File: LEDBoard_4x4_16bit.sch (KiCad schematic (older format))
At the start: 34 parts, among them J1 VCC_in, J2 GND_in, J3 signal_in, J4 VCC_out, J5 GND_out, J6 signal_out, U1 TLC5971RGER, U2 TLC5971RGER, U3 TLC5971RGER, U4 TLC5971RGER

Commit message: pcb parts all positioned
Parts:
- removed J2: GND_in, Socket_Strips:Socket_Strip_Angled_1x01_Pitch2.54mm, symbol CONN_01X01_MALE
- removed J4: VCC_out, Socket_Strips:Socket_Strip_Angled_1x01_Pitch2.54mm, symbol CONN_01X01_FEMALE
- removed J5: GND_out, Socket_Strips:Socket_Strip_Angled_1x01_Pitch2.54mm, symbol CONN_01X01_FEMALE
- added C5: 47uF, Capacitors_SMD:C_0603, symbol C
- added HS1: Heatsink, Oddities:Dummy_Empty, symbol Heatsink
- added MK1, MK2: Mounting_Hole, Mounting_Holes:MountingHole_2.7mm_M2.5_Pad_Via, symbol Mounting_Hole_PAD
- C1: YAGEO (none) -> CC0603KRX7R7BB104; reichelt (none) -> X7R-G0603 100N; reichelt_url (none) -> https://www.reichelt.de/Vielschicht-SMD-G0603/X7R-G0603-100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
- J2: renamed from J1; value VCC_in -> power; footprint Socket_Strips:Socket_Strip_Angled_1x01_Pitch2.54mm -> Socket_Strips:Socket_Strip_Straight_1x06_Pitch2.54mm; symbol CONN_01X01_MALE -> CONN_01X06
- J6: footprint Socket_Strips:Socket_Strip_Angled_1x02_Pitch2.54mm -> Socket_Strips:Socket_Strip_Straight_1x02_Pitch2.54mm
- R1: value R -> 2k7 1%; YAGEO (none) -> RC0603FR-072K7L; reichelt (none) -> SMD-0603 2,7K; reichelt_url (none) -> https://www.reichelt.de/SMD-0603-von-1-bis-910-kOhm/SMD-060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
- U1, U2, U3, U4: footprint Housings_DFN_QFN:QFN-24-1EP_4x4mm_Pitch0.5mm -> Housings_DFN_QFN:Texas_S-PVQFN-N24_ThermalVias
- renumbered J3 to J1
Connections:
- wire segments 66 -> 74
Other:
- moved on the sheet: J1, J6

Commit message: pcb started routing
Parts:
- D1.1, D1.2, D1.3, D1.4, D2.1, D2.2, D2.3, D2.4, D3.1, D3.2, D3.3, D3.4, D4.1, D4.2, D4.3, D4.4: footprint nichia:LED_NSSM032AT_wViaHeatSink -> nichia:LED_NSSM032AT_wViaHeatSinkBig
- MK1, MK2: footprint Mounting_Holes:MountingHole_2.7mm_M2.5_Pad_Via -> Mounting_Holes:MountingHole_3.2mm_M3_ISO7380_Pad
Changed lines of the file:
@@
 F 0 "D1.1" H 3950 2047 50  0000 C CNN
 F 1 "LED_1.1" H 3950 1956 50  0000 C CNN
-F 2 "nichia:LED_NSSM032AT_wViaHeatSink" H 3950 1500 50  0001 C CNN
+F 2 "nichia:LED_NSSM032AT_wViaHeatSinkBig" H 3950 1500 50  0001 C CNN
 F 3 "" H 3950 1500 50  0001 C CNN
 F 4 "NSSM032A" H 3950 1550 60  0001 C CNN "Nichia part"
@@
 F 0 "D1.2" H 3950 2947 50  0000 C CNN
 F 1 "LED_1.2" H 3950 2856 50  0000 C CNN
-F 2 "nichia:LED_NSSM032AT_wViaHeatSink" H 3950 2400 50  0001 C CNN
+F 2 "nichia:LED_NSSM032AT_wViaHeatSinkBig" H 3950 2400 50  0001 C CNN
 F 3 "" H 3950 2400 50  0001 C CNN
 F 4 "NSSM032A" H 3950 2450 60  0001 C CNN "Nichia part"
@@
 F 0 "D2.1" H 5150 2047 50  0000 C CNN
 F 1 "LED_2.1" H 5150 1956 50  0000 C CNN
-F 2 "nichia:LED_NSSM032AT_wViaHeatSink" H 5150 1500 50  0001 C CNN
+F 2 "nichia:LED_NSSM032AT_wViaHeatSinkBig" H 5150 1500 50  0001 C CNN
 F 3 "" H 5150 1500 50  0001 C CNN
 F 4 "NSSM032A" H 5150 1550 60  0001 C CNN "Nichia part"
@@
 F 0 "D2.2" H 5150 2947 50  0000 C CNN
 F 1 "LED_2.2" H 5150 2856 50  0000 C CNN
-F 2 "nichia:LED_NSSM032AT_wViaHeatSink" H 5150 2400 50  0001 C CNN
+F 2 "nichia:LED_NSSM032AT_wViaHeatSinkBig" H 5150 2400 50  0001 C CNN
 F 3 "" H 5150 2400 50  0001 C CNN
 F 4 "NSSM032A" H 5150 2450 60  0001 C CNN "Nichia part"
@@
 F 0 "D3.1" H 9250 2047 50  0000 C CNN
 F 1 "LED_3.1" H 9250 1956 50  0000 C CNN
-F 2 "nichia:LED_NSSM032AT_wViaHeatSink" H 9250 1500 50  0001 C CNN
+F 2 "nichia:LED_NSSM032AT_wViaHeatSinkBig" H 9250 1500 50  0001 C CNN
 F 3 "" H 9250 1500 50  0001 C CNN
 F 4 "NSSM032A" H 9250 1550 60  0001 C CNN "Nichia part"
@@
 F 0 "D3.2" H 9250 2947 50  0000 C CNN
 F 1 "LED_3.2" H 9250 2856 50  0000 C CNN
-F 2 "nichia:LED_NSSM032AT_wViaHeatSink" H 9250 2400 50  0001 C CNN
+F 2 "nichia:LED_NSSM032AT_wViaHeatSinkBig" H 9250 2400 50  0001 C CNN
 F 3 "" H 9250 2400 50  0001 C CNN
 F 4 "NSSM032A" H 9250 2450 60  0001 C CNN "Nichia part"
@@
 F 0 "D4.1" H 10450 2047 50  0000 C CNN
 F 1 "LED_4.1" H 10450 1956 50  0000 C CNN
-F 2 "nichia:LED_NSSM032AT_wViaHeatSink" H 10450 1500 50  0001 C CNN
+F 2 "nichia:LED_NSSM032AT_wViaHeatSinkBig" H 10450 1500 50  0001 C CNN
 F 3 "" H 10450 1500 50  0001 C CNN
 F 4 "NSSM032A" H 10450 1550 60  0001 C CNN "Nichia part"
@@
 F 0 "D4.2" H 10450 2947 50  0000 C CNN
 F 1 "LED_4.2" H 10450 2856 50  0000 C CNN
-F 2 "nichia:LED_NSSM032AT_wViaHeatSink" H 10450 2400 50  0001 C CNN
+F 2 "nichia:LED_NSSM032AT_wViaHeatSinkBig" H 10450 2400 50  0001 C CNN
 F 3 "" H 10450 2400 50  0001 C CNN
 F 4 "NSSM032A" H 10450 2450 60  0001 C CNN "Nichia part"
@@
 F 0 "D1.3" H 3950 4797 50  0000 C CNN
 F 1 "LED_1.3" H 3950 4706 50  0000 C CNN
-F 2 "nichia:LED_NSSM032AT_wViaHeatSink" H 3950 4250 50  0001 C CNN
+F 2 "nichia:LED_NSSM032AT_wViaHeatSinkBig" H 3950 4250 50  0001 C CNN
 F 3 "" H 3950 4250 50  0001 C CNN
 F 4 "NSSM032A" H 3950 4300 60  0001 C CNN "Nichia part"
@@
 F 0 "D1.4" H 3950 5697 50  0000 C CNN
 F 1 "LED_1.4" H 3950 5606 50  0000 C CNN
-F 2 "nichia:LED_NSSM032AT_wViaHeatSink" H 3950 5150 50  0001 C CNN
+F 2 "nichia:LED_NSSM032AT_wViaHeatSinkBig" H 3950 5150 50  0001 C CNN
 F 3 "" H 3950 5150 50  0001 C CNN
 F 4 "NSSM032A" H 3950 5200 60  0001 C CNN "Nichia part"
@@
 F 0 "D2.3" H 5150 4797 50  0000 C CNN
 F 1 "LED_2.3" H 5150 4706 50  0000 C CNN
-F 2 "nichia:LED_NSSM032AT_wViaHeatSink" H 5150 4250 50  0001 C CNN
+F 2 "nichia:LED_NSSM032AT_wViaHeatSinkBig" H 5150 4250 50  0001 C CNN
 F 3 "" H 5150 4250 50  0001 C CNN
 F 4 "NSSM032A" H 5150 4300 60  0001 C CNN "Nichia part"
@@
 F 0 "D2.4" H 5150 5697 50  0000 C CNN
 F 1 "LED_2.4" H 5150 5606 50  0000 C CNN
-F 2 "nichia:LED_NSSM032AT_wViaHeatSink" H 5150 5150 50  0001 C CNN
+F 2 "nichia:LED_NSSM032AT_wViaHeatSinkBig" H 5150 5150 50  0001 C CNN
 F 3 "" H 5150 5150 50  0001 C CNN
 F 4 "NSSM032A" H 5150 5200 60  0001 C CNN "Nichia part"
@@
 F 0 "D3.3" H 9250 4797 50  0000 C CNN
 F 1 "LED_3.3" H 9250 4706 50  0000 C CNN
-F 2 "nichia:LED_NSSM032AT_wViaHeatSink" H 9250 4250 50  0001 C CNN
+F 2 "nichia:LED_NSSM032AT_wViaHeatSinkBig" H 9250 4250 50  0001 C CNN
 F 3 "" H 9250 4250 50  0001 C CNN
 F 4 "NSSM032A" H 9250 4300 60  0001 C CNN "Nichia part"
@@
 F 0 "D3.4" H 9250 5697 50  0000 C CNN
 F 1 "LED_3.4" H 9250 5606 50  0000 C CNN
-F 2 "nichia:LED_NSSM032AT_wViaHeatSink" H 9250 5150 50  0001 C CNN
+F 2 "nichia:LED_NSSM032AT_wViaHeatSinkBig" H 9250 5150 50  0001 C CNN
 F 3 "" H 9250 5150 50  0001 C CNN
 F 4 "NSSM032A" H 9250 5200 60  0001 C CNN "Nichia part"
@@
 F 0 "D4.3" H 10450 4797 50  0000 C CNN
 F 1 "LED_4.3" H 10450 4706 50  0000 C CNN
-F 2 "nichia:LED_NSSM032AT_wViaHeatSink" H 10450 4250 50  0001 C CNN
+F 2 "nichia:LED_NSSM032AT_wViaHeatSinkBig" H 10450 4250 50  0001 C CNN
 F 3 "" H 10450 4250 50  0001 C CNN
 F 4 "NSSM032A" H 10450 4300 60  0001 C CNN "Nichia part"
@@
 F 0 "D4.4" H 10450 5697 50  0000 C CNN
 F 1 "LED_4.4" H 10450 5606 50  0000 C CNN
-F 2 "nichia:LED_NSSM032AT_wViaHeatSink" H 10450 5150 50  0001 C CNN
+F 2 "nichia:LED_NSSM032AT_wViaHeatSinkBig" H 10450 5150 50  0001 C CNN
 F 3 "" H 10450 5150 50  0001 C CNN
 F 4 "NSSM032A" H 10450 5200 60  0001 C CNN "Nichia part"
@@
 F 0 "MK1" H 4050 6051 50  0000 L CNN
 F 1 "Mounting_Hole" H 4050 5960 50  0000 L CNN
-F 2 "Mounting_Holes:MountingHole_2.7mm_M2.5_Pad_Via" H 3950 6000 50  0001 C CNN
+F 2 "Mounting_Holes:MountingHole_3.2mm_M3_ISO7380_Pad" H 3950 6000 50  0001 C CNN
 F 3 "" H 3950 6000 50  0001 C CNN
 	1    3950 6000
@@
 $EndComp
 $Comp
-L GND #PWR053
+L GND #PWR051
 U 1 1 596BEB36
 P 3950 6100
-F 0 "#PWR053" H 3950 5850 50  0001 C CNN
+F 0 "#PWR051" H 3950 5850 50  0001 C CNN
 F 1 "GND" H 3955 5927 50  0000 C CNN
 F 2 "" H 3950 6100 50  0001 C CNN
@@
 F 0 "MK2" H 4800 6051 50  0000 L CNN
 F 1 "Mounting_Hole" H 4800 5960 50  0000 L CNN
-F 2 "Mounting_Holes:MountingHole_2.7mm_M2.5_Pad_Via" H 4700 6000 50  0001 C CNN
+F 2 "Mounting_Holes:MountingHole_3.2mm_M3_ISO7380_Pad" H 4700 6000 50  0001 C CNN
 F 3 "" H 4700 6000 50  0001 C CNN
 	1    4700 6000
@@
 $EndComp
 $Comp
-L GND #PWR054
+L GND #PWR052
 U 1 1 596BF4D1
 P 4700 6100
-F 0 "#PWR054" H 4700 5850 50  0001 C CNN
+F 0 "#PWR052" H 4700 5850 50  0001 C CNN
 F 1 "GND" H 4705 5927 50  0000 C CNN
 F 2 "" H 4700 6100 50  0001 C CNN

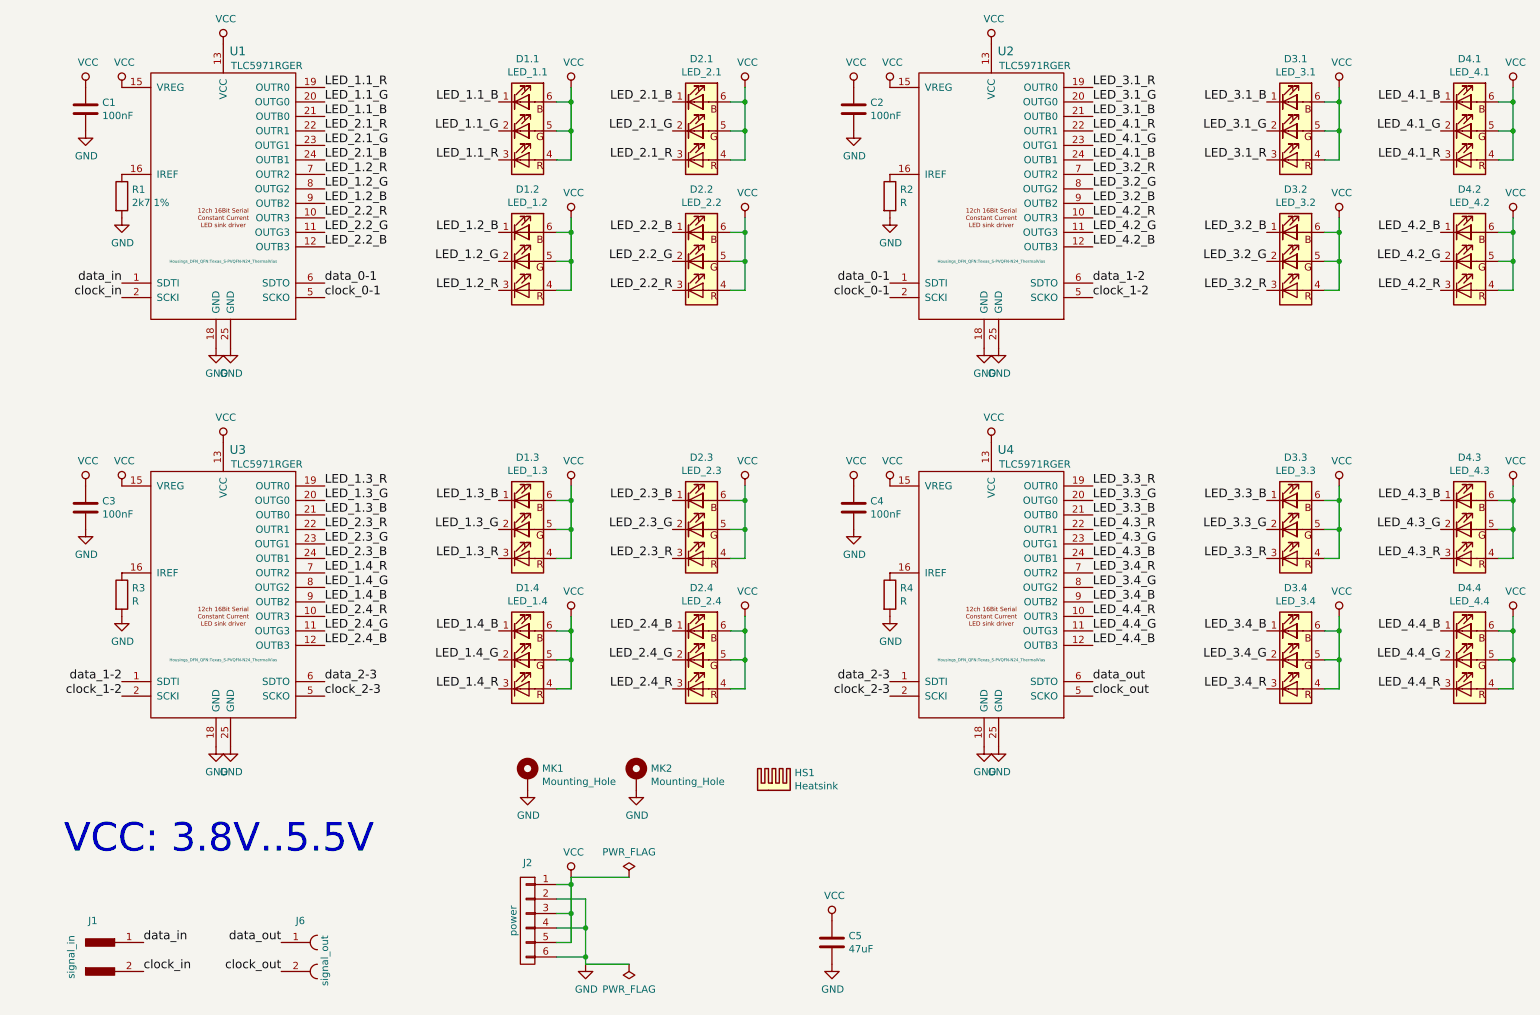
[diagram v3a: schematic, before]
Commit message: pcb tried to fix missing net links
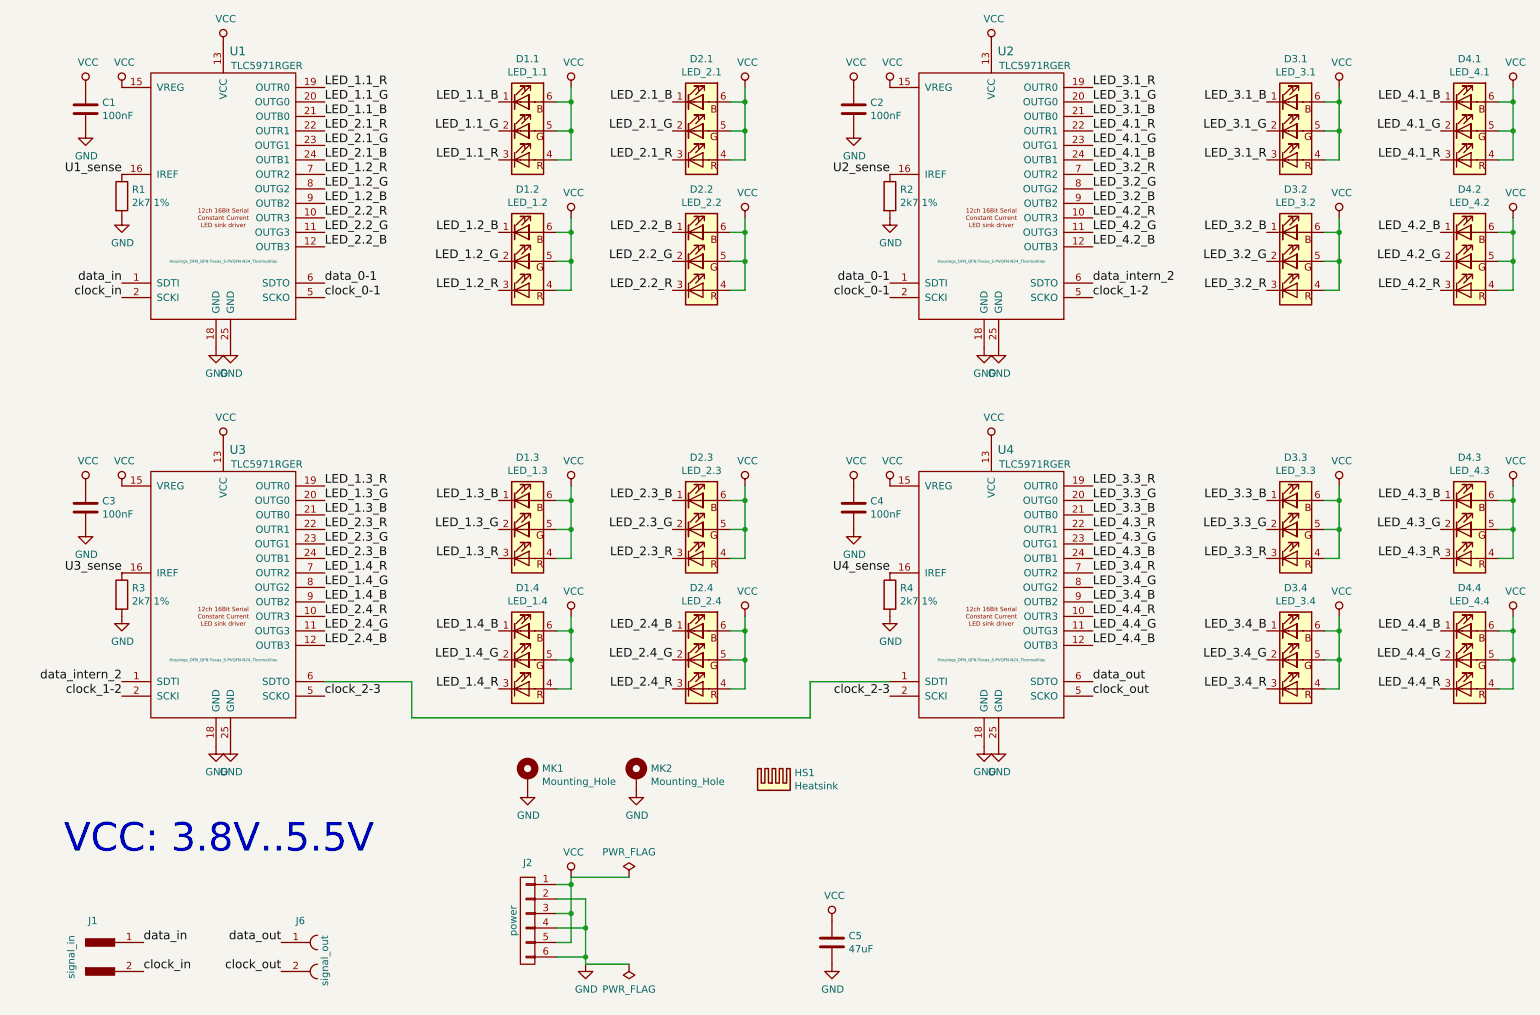
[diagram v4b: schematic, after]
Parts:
- C2, C3, C4: YAGEO (none) -> CC0603KRX7R7BB104; reichelt (none) -> X7R-G0603 100N; reichelt_url (none) -> https://www.reichelt.de/Vielschicht-SMD-G0603/X7R-G0603-100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
- R2, R3, R4: value R -> 2k7 1%; YAGEO (none) -> RC0603FR-072K7L; reichelt (none) -> SMD-0603 2,7K; reichelt_url (none) -> https://www.reichelt.de/SMD-0603-von-1-bis-910-kOhm/SMD-060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
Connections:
- net data_1-2 is gone; now on net data_intern_2: U2.6 (SDTO), U3.1 (SDTI)
- net U1_sense: now reaches R1.1, U1.16 (IREF)
- net U2_sense: now reaches R2.1, U2.16 (IREF)
- net data_intern_2: now reaches U2.6 (SDTO)
- net U3_sense: now reaches R3.1, U3.16 (IREF)
- net at U3.6 (SDTO): now also U4.1 (SDTI)
- net U4_sense: now reaches R4.1, U4.16 (IREF)
- removed net data_2-3: U3.6 (SDTO), U4.1 (SDTI)
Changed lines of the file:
@@
 P 6450 2000
 F 0 "R2" H 6520 2046 50  0000 L CNN
-F 1 "R" H 6520 1955 50  0000 L CNN
+F 1 "2k7 1%" H 6520 1955 50  0000 L CNN
 F 2 "Resistors_SMD:R_0603" V 6380 2000 50  0001 C CNN
 F 3 "" H 6450 2000 50  0001 C CNN
+F 4 "SMD-0603 2,7K" H 1150 2000 60  0001 C CNN "reichelt"
+F 5 "https://www.reichelt.de/SMD-0603-von-1-bis-910-kOhm/SMD-0603-2-7K/3/index.html?ACTION=3&GROUPID=7968&ARTICLE=89435&OFFSET=100&" H 1150 2000 60  0001 C CNN "reichelt_url"
+F 6 "RC0603FR-072K7L" H 1150 2000 60  0001 C CNN "YAGEO"
 	1    6450 2000
 	1    0    0    -1
@@
 F 2 "Capacitors_SMD:C_0603" H 6238 1250 50  0001 C CNN
 F 3 "" H 6200 1400 50  0001 C CNN
+F 4 "X7R-G0603 100N" H 0   0   60  0001 C CNN "reichelt"
+F 5 "https://www.reichelt.de/Vielschicht-SMD-G0603/X7R-G0603-100N/3/index.html?ACTION=3&GROUPID=3166&ARTICLE=31873&OFFSET=100&" H 0   0   60  0001 C CNN "reichelt_url"
+F 6 "CC0603KRX7R7BB104" H 0   0   60  0001 C CNN "YAGEO"
 	1    6200 1400
 	1    0    0    -1
@@
 P 1150 4750
 F 0 "R3" H 1220 4796 50  0000 L CNN
-F 1 "R" H 1220 4705 50  0000 L CNN
+F 1 "2k7 1%" H 1220 4705 50  0000 L CNN
 F 2 "Resistors_SMD:R_0603" V 1080 4750 50  0001 C CNN
 F 3 "" H 1150 4750 50  0001 C CNN
+F 4 "SMD-0603 2,7K" H 1150 2000 60  0001 C CNN "reichelt"
+F 5 "https://www.reichelt.de/SMD-0603-von-1-bis-910-kOhm/SMD-0603-2-7K/3/index.html?ACTION=3&GROUPID=7968&ARTICLE=89435&OFFSET=100&" H 1150 2000 60  0001 C CNN "reichelt_url"
+F 6 "RC0603FR-072K7L" H 1150 2000 60  0001 C CNN "YAGEO"
 	1    1150 4750
 	1    0    0    -1
@@
 F 2 "Capacitors_SMD:C_0603" H 938 4000 50  0001 C CNN
 F 3 "" H 900 4150 50  0001 C CNN
+F 4 "X7R-G0603 100N" H 0   0   60  0001 C CNN "reichelt"
+F 5 "https://www.reichelt.de/Vielschicht-SMD-G0603/X7R-G0603-100N/3/index.html?ACTION=3&GROUPID=3166&ARTICLE=31873&OFFSET=100&" H 0   0   60  0001 C CNN "reichelt_url"
+F 6 "CC0603KRX7R7BB104" H 0   0   60  0001 C CNN "YAGEO"
 	1    900  4150
 	1    0    0    -1
@@
 P 6450 4750
 F 0 "R4" H 6520 4796 50  0000 L CNN
-F 1 "R" H 6520 4705 50  0000 L CNN
+F 1 "2k7 1%" H 6520 4705 50  0000 L CNN
 F 2 "Resistors_SMD:R_0603" V 6380 4750 50  0001 C CNN
 F 3 "" H 6450 4750 50  0001 C CNN
+F 4 "SMD-0603 2,7K" H 1150 2000 60  0001 C CNN "reichelt"
+F 5 "https://www.reichelt.de/SMD-0603-von-1-bis-910-kOhm/SMD-0603-2-7K/3/index.html?ACTION=3&GROUPID=7968&ARTICLE=89435&OFFSET=100&" H 1150 2000 60  0001 C CNN "reichelt_url"
+F 6 "RC0603FR-072K7L" H 1150 2000 60  0001 C CNN "YAGEO"
 	1    6450 4750
 	1    0    0    -1
@@
 F 2 "Capacitors_SMD:C_0603" H 6238 4000 50  0001 C CNN
 F 3 "" H 6200 4150 50  0001 C CNN
+F 4 "X7R-G0603 100N" H 0   0   60  0001 C CNN "reichelt"
+F 5 "https://www.reichelt.de/Vielschicht-SMD-G0603/X7R-G0603-100N/3/index.html?ACTION=3&GROUPID=3166&ARTICLE=31873&OFFSET=100&" H 0   0   60  0001 C CNN "reichelt_url"
+F 6 "CC0603KRX7R7BB104" H 0   0   60  0001 C CNN "YAGEO"
 	1    6200 4150
 	1    0    0    -1
@@
 Text Label 1300 7350 0    60   ~ 0
 clock_in
-Text Label 7850 2600 0    60   ~ 0
-data_1-2
 Text Label 7850 2700 0    60   ~ 0
 clock_1-2
-Text Label 1150 5350 2    60   ~ 0
-data_1-2
 Text Label 1150 5450 2    60   ~ 0
 clock_1-2
 Text Label 2550 5450 0    60   ~ 0
 clock_2-3
-Text Label 6450 5350 2    60   ~ 0
-data_2-3
 Text Label 6450 5450 2    60   ~ 0
 clock_2-3
@@
 Text Label 2250 7150 2    60   ~ 0
 data_out
-Text Label 2550 5350 0    60   ~ 0
-data_2-3
+Text Label 7850 2600 0    60   ~ 0
+data_intern_2
+Text Label 6450 1850 2    60   ~ 0
+U2_sense
+Text Label 1150 1850 2    60   ~ 0
+U1_sense
+Text Label 1150 4600 2    60   ~ 0
+U3_sense
+Text Label 6450 4600 2    60   ~ 0
+U4_sense
+Wire Wire Line
+	2550 5350 3150 5350
+Wire Wire Line
+	3150 5350 3150 5600
+Wire Wire Line
+	3150 5600 5900 5600
+Wire Wire Line
+	5900 5600 5900 5350
+Wire Wire Line
+	5900 5350 6450 5350
+Text Label 1150 5350 2    60   ~ 0
+data_intern_2
 $EndSCHEMATC

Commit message: updated net labeling
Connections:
- net data_intern_2 is gone; now on net data_1-2: U2.6 (SDTO), U3.1 (SDTI)
- net data_1-2: now reaches U2.6 (SDTO)
- net data_2-3: now reaches U3.6 (SDTO)
- net data_2-3: now also U4.1 (SDTI)
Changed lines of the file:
@@
 data_out
 Text Label 7850 2600 0    60   ~ 0
-data_intern_2
+data_1-2
 Text Label 6450 1850 2    60   ~ 0
 U2_sense
@@
 	5900 5350 6450 5350
 Text Label 1150 5350 2    60   ~ 0
-data_intern_2
+data_1-2
+Text Label 2550 5350 0    60   ~ 0
+data_2-3
 $EndSCHEMATC

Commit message: fixed net data_1-2 (manually hand edited net-file)
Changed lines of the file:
@@
 Text Label 6450 4600 2    60   ~ 0
 U4_sense
+Text Label 2550 5350 0    60   ~ 0
+data_2-3
 Wire Wire Line
-	2550 5350 3150 5350
+	1150 5350 650  5350
+Wire Wire Line
+	650  5350 650  3350
+Wire Wire Line
+	650  3350 8400 3350
+Wire Wire Line
+	8400 3350 8400 2600
+Wire Wire Line
+	8400 2600 7850 2600
+Wire Wire Line
+	5900 5350 6450 5350
+Wire Wire Line
+	5900 5600 5900 5350
+Wire Wire Line
+	3150 5600 5900 5600
 Wire Wire Line
 	3150 5350 3150 5600
 Wire Wire Line
-	3150 5600 5900 5600
-Wire Wire Line
-	5900 5600 5900 5350
-Wire Wire Line
-	5900 5350 6450 5350
-Text Label 1150 5350 2    60   ~ 0
-data_1-2
-Text Label 2550 5350 0    60   ~ 0
-data_2-3
+	2550 5350 3150 5350
 $EndSCHEMATC
